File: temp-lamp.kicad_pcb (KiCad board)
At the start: 2 copper layers, 46.7 x 64.7 mm, 29 parts, among them M2 M3, M3 M3, P1 USB_5PIN_SHELL, P4 LED_1, P5 CONN_01X04, SW1 ON/OFF, SW2 RESET, SW3 PGM, U1 MCP73831, U2 ESP-12E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

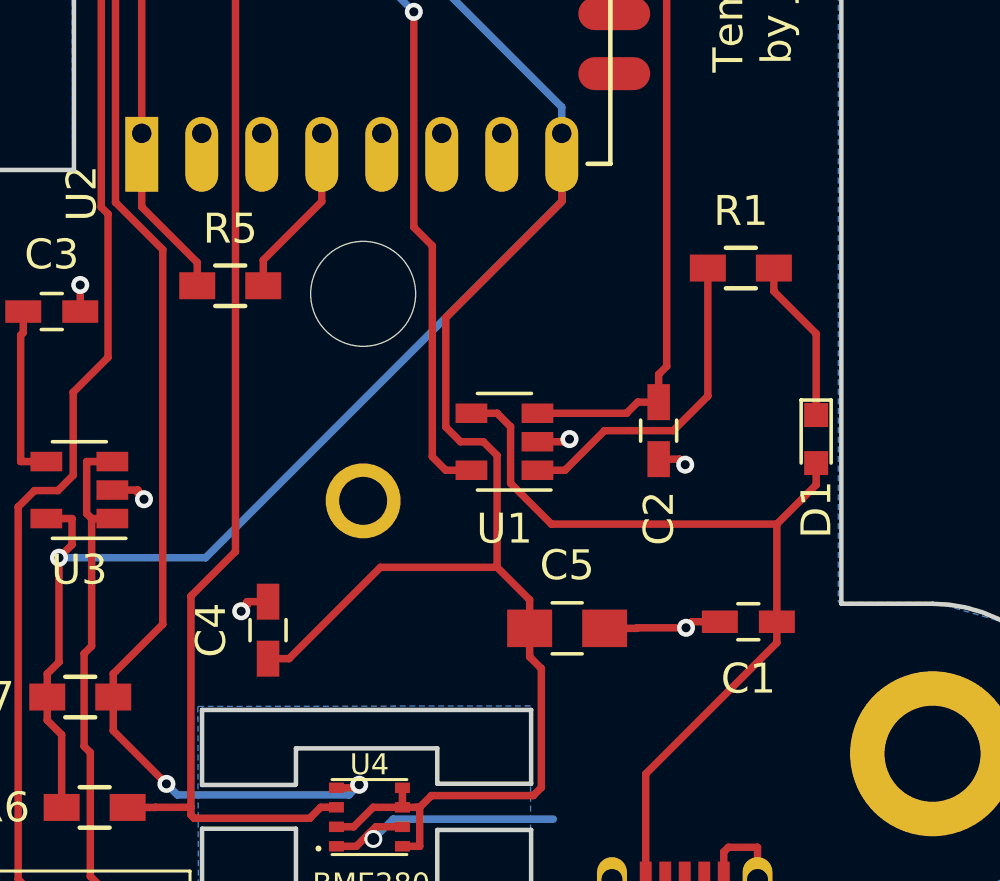
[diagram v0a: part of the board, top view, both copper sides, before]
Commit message: Shuffled some capacitors around
to make @projectgus happy...
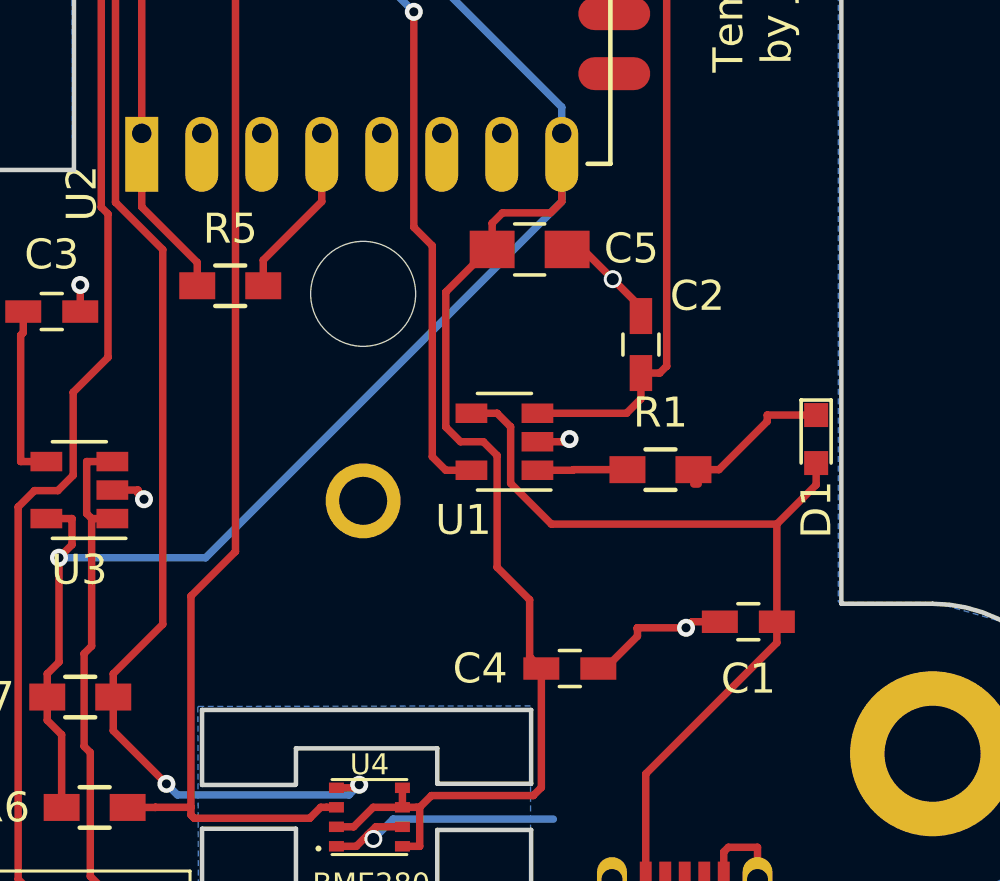
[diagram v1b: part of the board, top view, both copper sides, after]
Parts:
- moved C5 12.7 mm to (233.2, 110.2)
- moved C4 10.1 mm to (234.6, 124.2), turned to 0 degrees
- moved R1 7.23 mm to (237.6, 117.5)
- moved C2 2.93 mm to (236.9, 113.4), turned to 90 degrees
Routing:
- net Net-(R1-Pad1): track 11.0 -> 3.01 mm
- net +3V3: track 124.1 -> 116.2 mm
- net GND: track 24.8 -> 27.2 mm, vias 10 -> 9

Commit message: Updated pcb.
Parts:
- C5: footprint Capacitors_SMD:C_0805_HandSoldering -> Capacitors_SMD:C_1206_HandSoldering
- R3, R4: value 470 -> 10K
- SW1: value ON/OFF -> ON|OFF
- U3: value SPX3819M5 -> SPX3819M5-3.3
- moved D2 42.4 mm to (232.6, 115.0), turned to 270 degrees
- moved F1 38.7 mm to (229.7, 122.1), turned to 180 degrees
- moved R4 25.6 mm to (223.4, 109.9), turned to 180 degrees
- moved U1 7.95 mm to (239.4, 120.4), turned to 270 degrees
- moved R1 5.31 mm to (241.1, 113.5)
- moved C5 4.57 mm to (237.8, 109.7)
- moved C1 3.01 mm to (240.5, 125.6)
- moved SW3 2.87 mm to (241.8, 83.5)
- moved C2 1.96 mm to (237.5, 115.2)
- moved U3 1.75 mm to (217.4, 116.7), turned to 90 degrees
- moved C4 1.63 mm to (235.4, 125.6)
- moved P5 1.46 mm to (216.2, 79.7)
- moved R5 1.09 mm to (223.4, 112.5)
- moved C3 0.82 mm to (216.6, 111.8), turned to 180 degrees
- moved R6 0.46 mm to (218.3, 128.6)
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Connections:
- D2 pad 1: Net-(C2-Pad1) -> GND
- D2 pad 2: GND -> Net-(C2-Pad1)
- R3 pad 2: Net-(R3-Pad2) -> +3V3
- R4 pad 1: /GPIO0 -> /ENABLE
- R4 pad 2: Net-(R4-Pad2) -> +3V3
- SW2 pad 2: Net-(R3-Pad2) -> /RESET
- SW3 pad 2: Net-(R4-Pad2) -> /GPIO0
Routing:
- net Net-(C2-Pad1): track 63.1 -> 16.1 mm
- net /BAT_V: track 58.8 -> 19.9 mm, vias 0 -> 1
- net +3V3: track 116.2 -> 140.1 mm, vias 1 -> 3
- net Net-(R2-Pad1): track 19.4 -> 30.8 mm
- net /RESET: track 37.5 -> 46.3 mm, vias 0 -> 2
- net /GPIO0: track 8.60 -> 17.3 mm
- net +5V: track 29.1 -> 22.0 mm
- net Net-(R4-Pad2): track 4.42 -> 0.00 mm
- net Net-(R3-Pad2): track 4.34 -> 0.00 mm
- net /ENABLE: track 0.00 -> 3.65 mm
- net Net-(SW1-Pad1): track 17.9 -> 21.0 mm
- net /I2C_SCL: track 47.3 -> 50.4 mm, vias 2 -> 0
- net /I2C_SDA: track 45.7 -> 48.6 mm, vias 0 -> 2
- net Net-(R1-Pad1): track 3.01 -> 5.91 mm
- net Net-(D1-Pad1): track 5.12 -> 2.52 mm
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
